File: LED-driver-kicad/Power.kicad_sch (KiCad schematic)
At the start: 32 parts, among them U1 PD70210A, U3 LV2862XLVDDCR, U4 LV2862XLVDDCR

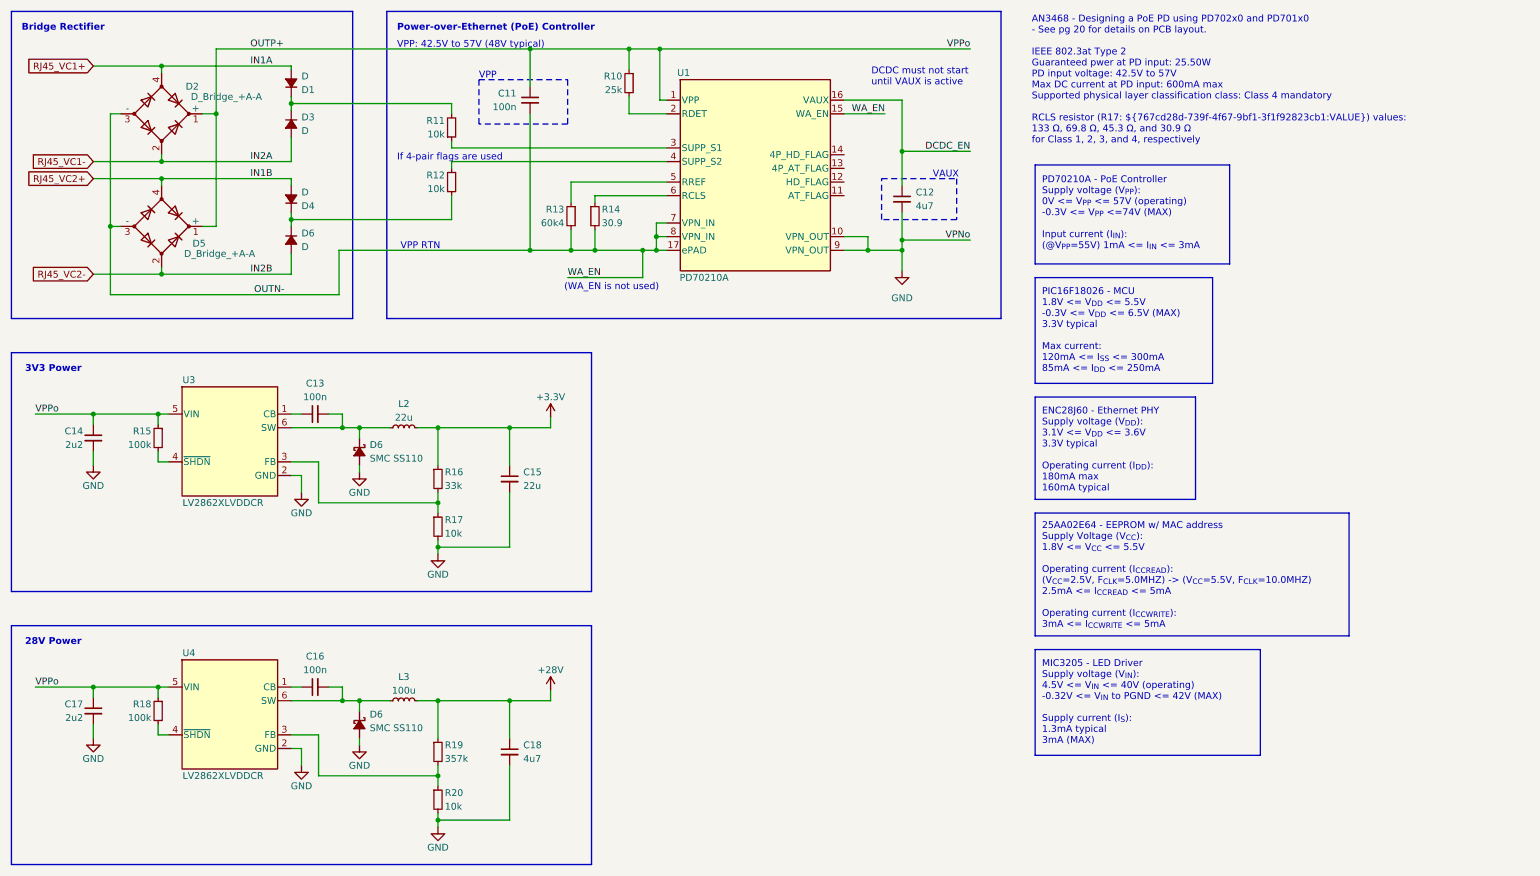
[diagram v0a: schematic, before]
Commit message: resolve Electrical Rules Checker (ERC) errors and warnings
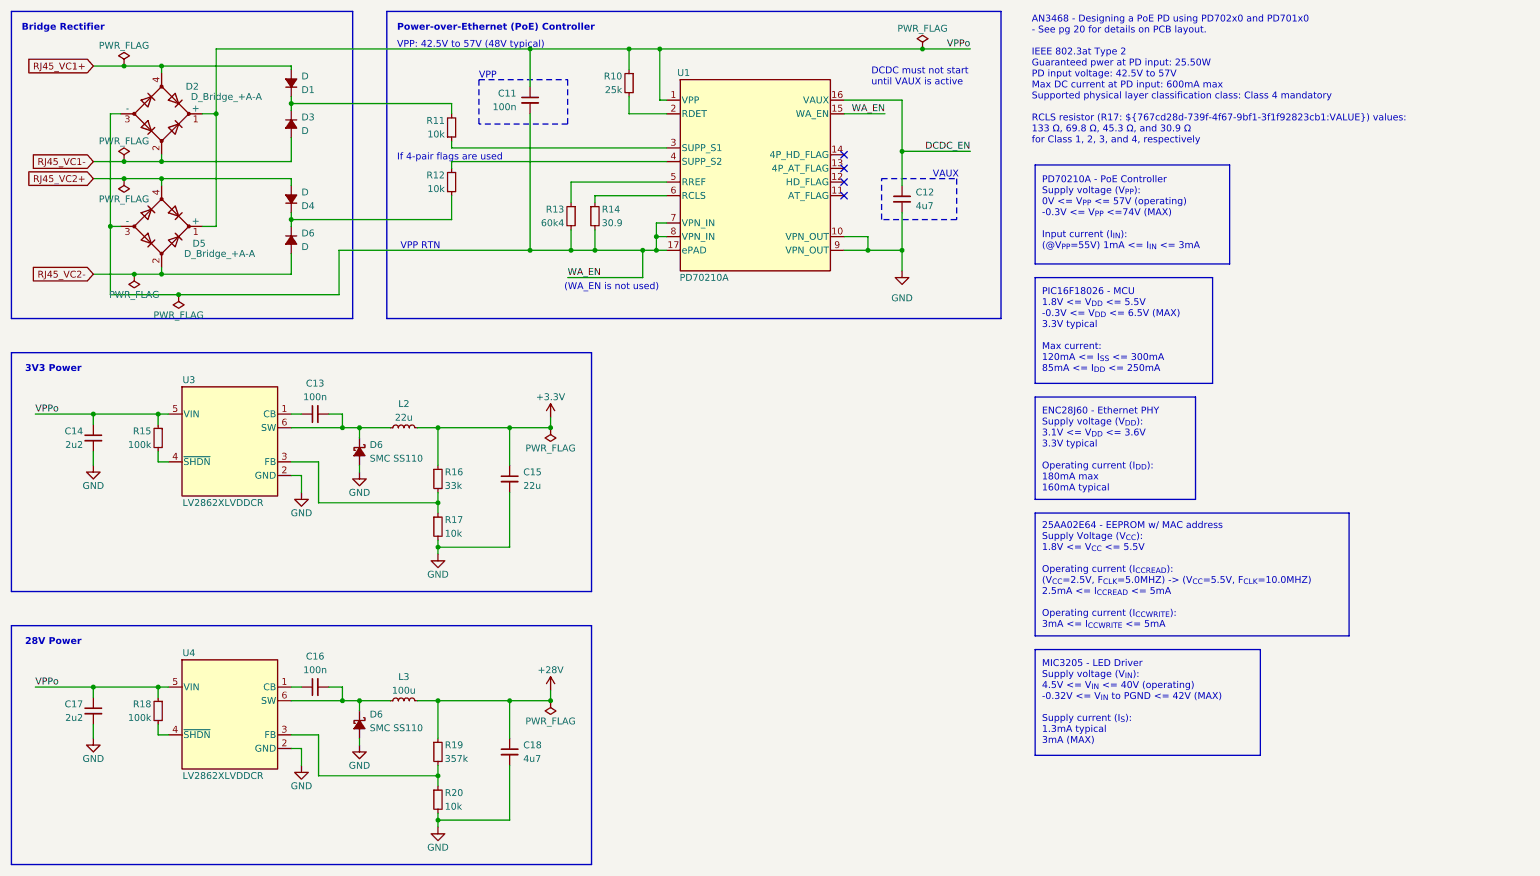
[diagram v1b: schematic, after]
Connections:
- net OUTN- renamed WA_EN
- net OUTP+ renamed VPPo
- no-connect marks 0 -> 4

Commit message: update footprint assignments
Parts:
- C11, C13, C16: footprint (none) -> Capacitor_SMD:C_0402_1005Metric
- C12, C15, C18: footprint (none) -> Capacitor_SMD:C_0805_2012Metric
- C14, C17: footprint (none) -> Capacitor_SMD:C_1206_3216Metric
- L2: footprint (none) -> Inductor_SMD:L_1210_3225Metric
- L3: footprint (none) -> Inductor_SMD:L_TDK_VLS4015CX-6R8M-H
- R10, R11, R12, R13, R14, R15, R16, R17, R18, R19, R20: footprint (none) -> Resistor_SMD:R_0402_1005Metric
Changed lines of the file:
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@@
       (effects (font (size 1.27 1.27)) (justify right))
     )
-    (property "Footprint" "" (at 100.965 50.8 0)
+    (property "Footprint" "Resistor_SMD:R_0402_1005Metric" (at 100.965 50.8 0)
       (effects (font (size 1.27 1.27)) hide)
     )
@@
       (effects (font (size 1.27 1.27)) (justify left))
     )
-    (property "Footprint" "" (at 98.425 165.735 0)
+    (property "Footprint" "Resistor_SMD:R_0402_1005Metric" (at 98.425 165.735 0)
       (effects (font (size 1.27 1.27)) hide)
     )
@@
       (effects (font (size 1.27 1.27)) (justify left))
     )
-    (property "Footprint" "" (at 98.425 114.935 0)
+    (property "Footprint" "Resistor_SMD:R_0402_1005Metric" (at 98.425 114.935 0)
       (effects (font (size 1.27 1.27)) hide)
     )
@@
       (effects (font (size 1.27 1.27)) (justify left))
     )
-    (property "Footprint" "" (at 111.76 106.045 0)
+    (property "Footprint" "Capacitor_SMD:C_0805_2012Metric" (at 111.76 106.045 0)
       (effects (font (size 1.27 1.27)) hide)
     )
@@
       (effects (font (size 1.27 1.27)) (justify left))
     )
-    (property "Footprint" "" (at 98.425 106.045 0)
+    (property "Footprint" "Resistor_SMD:R_0402_1005Metric" (at 98.425 106.045 0)
       (effects (font (size 1.27 1.27)) hide)
     )
@@
       (effects (font (size 1.27 1.27)) (justify right))
     )
-    (property "Footprint" "" (at 34.29 149.225 0)
+    (property "Footprint" "Capacitor_SMD:C_1206_3216Metric" (at 34.29 149.225 0)
       (effects (font (size 1.27 1.27)) hide)
     )
@@
       (effects (font (size 1.27 1.27)))
     )
-    (property "Footprint" "" (at 92.075 147.32 0)
+    (property "Footprint" "Inductor_SMD:L_TDK_VLS4015CX-6R8M-H" (at 92.075 147.32 0)
       (effects (font (size 1.27 1.27)) hide)
     )
@@
       (effects (font (size 1.27 1.27)) (justify left))
     )
-    (property "Footprint" "" (at 133.985 32.385 0)
+    (property "Footprint" "Resistor_SMD:R_0402_1005Metric" (at 133.985 32.385 0)
       (effects (font (size 1.27 1.27)) hide)
     )
@@
       (effects (font (size 1.27 1.27)) (justify left))
     )
-    (property "Footprint" "" (at 46.355 98.425 0)
+    (property "Footprint" "Resistor_SMD:R_0402_1005Metric" (at 46.355 98.425 0)
       (effects (font (size 1.27 1.27)) hide)
     )
@@
       (effects (font (size 1.27 1.27)) (justify left))
     )
-    (property "Footprint" "" (at 127.635 57.15 0)
+    (property "Footprint" "Resistor_SMD:R_0402_1005Metric" (at 127.635 57.15 0)
       (effects (font (size 1.27 1.27)) hide)
     )
@@
       (effects (font (size 1.27 1.27)) (justify left))
     )
-    (property "Footprint" "" (at 46.355 149.225 0)
+    (property "Footprint" "Resistor_SMD:R_0402_1005Metric" (at 46.355 149.225 0)
       (effects (font (size 1.27 1.27)) hide)
     )
@@
       (effects (font (size 1.27 1.27)))
     )
-    (property "Footprint" "" (at 75.565 93.98 0)
+    (property "Footprint" "Capacitor_SMD:C_0402_1005Metric" (at 75.565 93.98 0)
       (effects (font (size 1.27 1.27)) hide)
     )
@@
       (effects (font (size 1.27 1.27)) (justify left))
     )
-    (property "Footprint" "" (at 115.57 35.56 0)
+    (property "Footprint" "Capacitor_SMD:C_0402_1005Metric" (at 115.57 35.56 0)
       (effects (font (size 1.27 1.27)) hide)
     )
@@
       (effects (font (size 1.27 1.27)) (justify left))
     )
-    (property "Footprint" "" (at 111.76 156.845 0)
+    (property "Footprint" "Capacitor_SMD:C_0805_2012Metric" (at 111.76 156.845 0)
       (effects (font (size 1.27 1.27)) hide)
     )
@@
       (effects (font (size 1.27 1.27)))
     )
-    (property "Footprint" "" (at 75.565 144.78 0)
+    (property "Footprint" "Capacitor_SMD:C_0402_1005Metric" (at 75.565 144.78 0)
       (effects (font (size 1.27 1.27)) hide)
     )
@@
       (effects (font (size 1.27 1.27)) (justify left))
     )
-    (property "Footprint" "" (at 184.785 53.975 0)
+    (property "Footprint" "Capacitor_SMD:C_0805_2012Metric" (at 184.785 53.975 0)
       (effects (font (size 1.27 1.27)) hide)
     )
@@
       (effects (font (size 1.27 1.27)) (justify right))
     )
-    (property "Footprint" "" (at 100.965 40.64 0)
+    (property "Footprint" "Resistor_SMD:R_0402_1005Metric" (at 100.965 40.64 0)
       (effects (font (size 1.27 1.27)) hide)
     )
@@
       (effects (font (size 1.27 1.27)) (justify left))
     )
-    (property "Footprint" "" (at 123.19 57.15 0)
+    (property "Footprint" "Resistor_SMD:R_0402_1005Metric" (at 123.19 57.15 0)
       (effects (font (size 1.27 1.27)) hide)
     )
@@
       (effects (font (size 1.27 1.27)))
     )
-    (property "Footprint" "" (at 92.075 96.52 0)
+    (property "Footprint" "Inductor_SMD:L_1210_3225Metric" (at 92.075 96.52 0)
       (effects (font (size 1.27 1.27)) hide)
     )
@@
       (effects (font (size 1.27 1.27)) (justify right))
     )
-    (property "Footprint" "" (at 34.29 98.425 0)
+    (property "Footprint" "Capacitor_SMD:C_1206_3216Metric" (at 34.29 98.425 0)
       (effects (font (size 1.27 1.27)) hide)
     )
@@
       (effects (font (size 1.27 1.27)) (justify left))
     )
-    (property "Footprint" "" (at 98.425 156.845 0)
-      (effects (font (size 1.27 1.27)) hide)
-    )
+    (property "Footprint" "Resistor_SMD:R_0402_1005Metric" (at 98.425 156.845 0)
+      (effects (font (size 1.27 1.27)) hide)
+    )

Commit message: update footprint assignments
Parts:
- D1, D3, D4, D6: footprint (none) -> Diode_SMD:D_SMA_Handsoldering
- D2, D5: footprint (none) -> KM-Diode_SMD:D_TO-269AA_4-BESOP_Diodes_MB10S-13
- D6: footprint (none) -> Diode_SMD:D_SMA
- L3: footprint Inductor_SMD:L_TDK_VLS4015CX-6R8M-H -> KM-Inductor_SMD:L_TDK_VLS4015CX-6R8M-H
- U1: footprint Package_DFN_QFN:DFN-16_5X4_MCH-Interface_PoE_Microchip_PD70210A -> KM-Package_DFN_QFN:DFN-16_5X4_MCH-Interface_PoE_Microchip_PD70210A
- U3, U4: footprint Package_SOT_SMD:SOT-23-Thin-6_DDC0006A-MFG_Regulator_Voltage_TI_LV2862XLVDDCR -> KM-Package_SOT_SMD:SOT-23-Thin-6_DDC0006A-MFG_Regulator_Voltage_TI_LV2862XLVDDCR
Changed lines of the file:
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@@
       (effects (font (size 1.27 1.27)) (justify left))
     )
-    (property "Footprint" "" (at 71.12 53.975 90)
+    (property "Footprint" "Diode_SMD:D_SMA_Handsoldering" (at 71.12 53.975 90)
       (effects (font (size 1.27 1.27)) hide)
     )
@@
       (effects (font (size 1.27 1.27)))
     )
-    (property "Footprint" "Package_DFN_QFN:DFN-16_5X4_MCH-Interface_PoE_Microchip_PD70210A" (at 157.48 49.53 0)
+    (property "Footprint" "KM-Package_DFN_QFN:DFN-16_5X4_MCH-Interface_PoE_Microchip_PD70210A" (at 157.48 49.53 0)
       (effects (font (size 1.27 1.27) italic) hide)
     )
@@
       (effects (font (size 1.27 1.27)) (justify left))
     )
-    (property "Footprint" "" (at 71.12 61.595 90)
+    (property "Footprint" "Diode_SMD:D_SMA_Handsoldering" (at 71.12 61.595 90)
       (effects (font (size 1.27 1.27)) hide)
     )
@@
       (effects (font (size 1.27 1.27)) (justify left))
     )
-    (property "Footprint" "" (at 71.12 32.385 90)
+    (property "Footprint" "Diode_SMD:D_SMA_Handsoldering" (at 71.12 32.385 90)
       (effects (font (size 1.27 1.27)) hide)
     )
@@
       (effects (font (size 1.27 1.27)))
     )
-    (property "Footprint" "Inductor_SMD:L_TDK_VLS4015CX-6R8M-H" (at 92.075 147.32 0)
+    (property "Footprint" "KM-Inductor_SMD:L_TDK_VLS4015CX-6R8M-H" (at 92.075 147.32 0)
       (effects (font (size 1.27 1.27)) hide)
     )
@@
       (effects (font (size 1.27 1.27)))
     )
-    (property "Footprint" "" (at 46.99 38.1 0)
+    (property "Footprint" "KM-Diode_SMD:D_TO-269AA_4-BESOP_Diodes_MB10S-13" (at 46.99 38.1 0)
       (effects (font (size 1.27 1.27)) hide)
     )
@@
       (effects (font (size 1.27 1.27)))
     )
-    (property "Footprint" "" (at 46.99 59.055 0)
+    (property "Footprint" "KM-Diode_SMD:D_TO-269AA_4-BESOP_Diodes_MB10S-13" (at 46.99 59.055 0)
       (effects (font (size 1.27 1.27)) hide)
     )
@@
       (effects (font (size 1.27 1.27)) (justify left))
     )
-    (property "Footprint" "" (at 71.12 40.005 90)
+    (property "Footprint" "Diode_SMD:D_SMA_Handsoldering" (at 71.12 40.005 90)
       (effects (font (size 1.27 1.27)) hide)
     )
@@
       (effects (font (size 1.27 1.27)))
     )
-    (property "Footprint" "Package_SOT_SMD:SOT-23-Thin-6_DDC0006A-MFG_Regulator_Voltage_TI_LV2862XLVDDCR" (at 59.69 99.06 0)
+    (property "Footprint" "KM-Package_SOT_SMD:SOT-23-Thin-6_DDC0006A-MFG_Regulator_Voltage_TI_LV2862XLVDDCR" (at 59.69 99.06 0)
       (effects (font (size 1.27 1.27) italic) hide)
     )
@@
       (effects (font (size 1.27 1.27)) (justify left))
     )
-    (property "Footprint" "" (at 83.82 100.965 90)
+    (property "Footprint" "Diode_SMD:D_SMA" (at 83.82 100.965 90)
       (effects (font (size 1.27 1.27)) hide)
     )
@@
       (effects (font (size 1.27 1.27)))
     )
-    (property "Footprint" "Package_SOT_SMD:SOT-23-Thin-6_DDC0006A-MFG_Regulator_Voltage_TI_LV2862XLVDDCR" (at 59.69 149.86 0)
+    (property "Footprint" "KM-Package_SOT_SMD:SOT-23-Thin-6_DDC0006A-MFG_Regulator_Voltage_TI_LV2862XLVDDCR" (at 59.69 149.86 0)
       (effects (font (size 1.27 1.27) italic) hide)
     )
@@
       (effects (font (size 1.27 1.27)) (justify left))
     )
-    (property "Footprint" "" (at 83.82 151.765 90)
-      (effects (font (size 1.27 1.27)) hide)
-    )
+    (property "Footprint" "Diode_SMD:D_SMA" (at 83.82 151.765 90)
+      (effects (font (size 1.27 1.27)) hide)
+    )

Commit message: add test points, net ties to schematics
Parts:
- added J2, J3: Conn_01x03_Socket, Connector_PinSocket_2.54mm:PinSocket_1x03_P2.54mm_Vertical, symbol Connector:Conn_01x03_Socket
- added NT1, NT2, NT3, NT4: NetTie_2, NetTie:NetTie-2_SMD_Pad0.5mm, symbol Device:NetTie_2
- added TP1, TP2, TP3, TP4: TestPoint, TestPoint:TestPoint_Pad_1.0x1.0mm, symbol Connector:TestPoint
- R18: renamed from R14; value 30.9 -> 30R9
- renumbered C17 to C11, C14 to C12, C16 to C13, C13 to C14, C11 to C15, C18 to C16, C15 to C17, C12 to C18, D2 to D1, D5 to D2, D1 to D3, D3 to D4, D4 to D5, L3 to L2, L2 to L3, R18 to R10, R19 to R13, R20 to R14, R16 to R15, R17 to R16, R13 to R17, R10 to R19, R15 to R9, U4 to U2
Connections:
- net GND: now also NT1.2, NT2.2, NT4.1; no longer C11.2, C12.2, C18.2, U1.10 (VPN_OUT), U1.9 (VPN_OUT)
- net WA_EN: now also NT3.2; no longer C15.2, D1.3 (-), D2.3 (-), R17.2, R18.2, U1.17 (ePAD), U1.7 (VPN_IN), U1.8 (VPN_IN)
- net at U3.4 (~{SHDN}): now also R9.1; no longer R9.2
- net at U2.4 (~{SHDN}): now also R10.1; no longer R10.2
- net DCDC_EN renamed VAUX
- net VAUX: now also J2.1 (Pin_1), J3.1 (Pin_1), TP3.1
- net VPPo renamed VPP
- net VPP: now also J2.3 (Pin_3), J3.3 (Pin_3), TP1.1; no longer R10.1, R9.1
- new net 28V_C_{IN}_GND: C11.2, NT1.1
- new net 28V_~{SHDN}: J3.2 (Pin_2), R10.2
- new net 3V3_C_{IN}_GND: C12.2, NT2.1
- new net 3V3_~{SHDN}: J2.2 (Pin_2), R9.2
- new net VPN_IN: C15.2, D1.3 (-), D2.3 (-), NT3.1, R17.2, R18.2, TP2.1, U1.17 (ePAD), U1.7 (VPN_IN), U1.8 (VPN_IN)
- new net VPN_OUT: C18.2, NT4.2, TP4.1, U1.10 (VPN_OUT), U1.9 (VPN_OUT)
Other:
- note added: "C_{IN}"
- note added: "C_{OUT}"
- note added: "WA_EN is not used"
- note removed: "(WA_EN is not used)"
- note removed: "VPP RTN"
- moved on the sheet: C11, C12, C13, C14, C16, C17, C18, D6, L2, L3, R10, R13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
